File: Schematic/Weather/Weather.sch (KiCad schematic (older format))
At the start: 0 parts

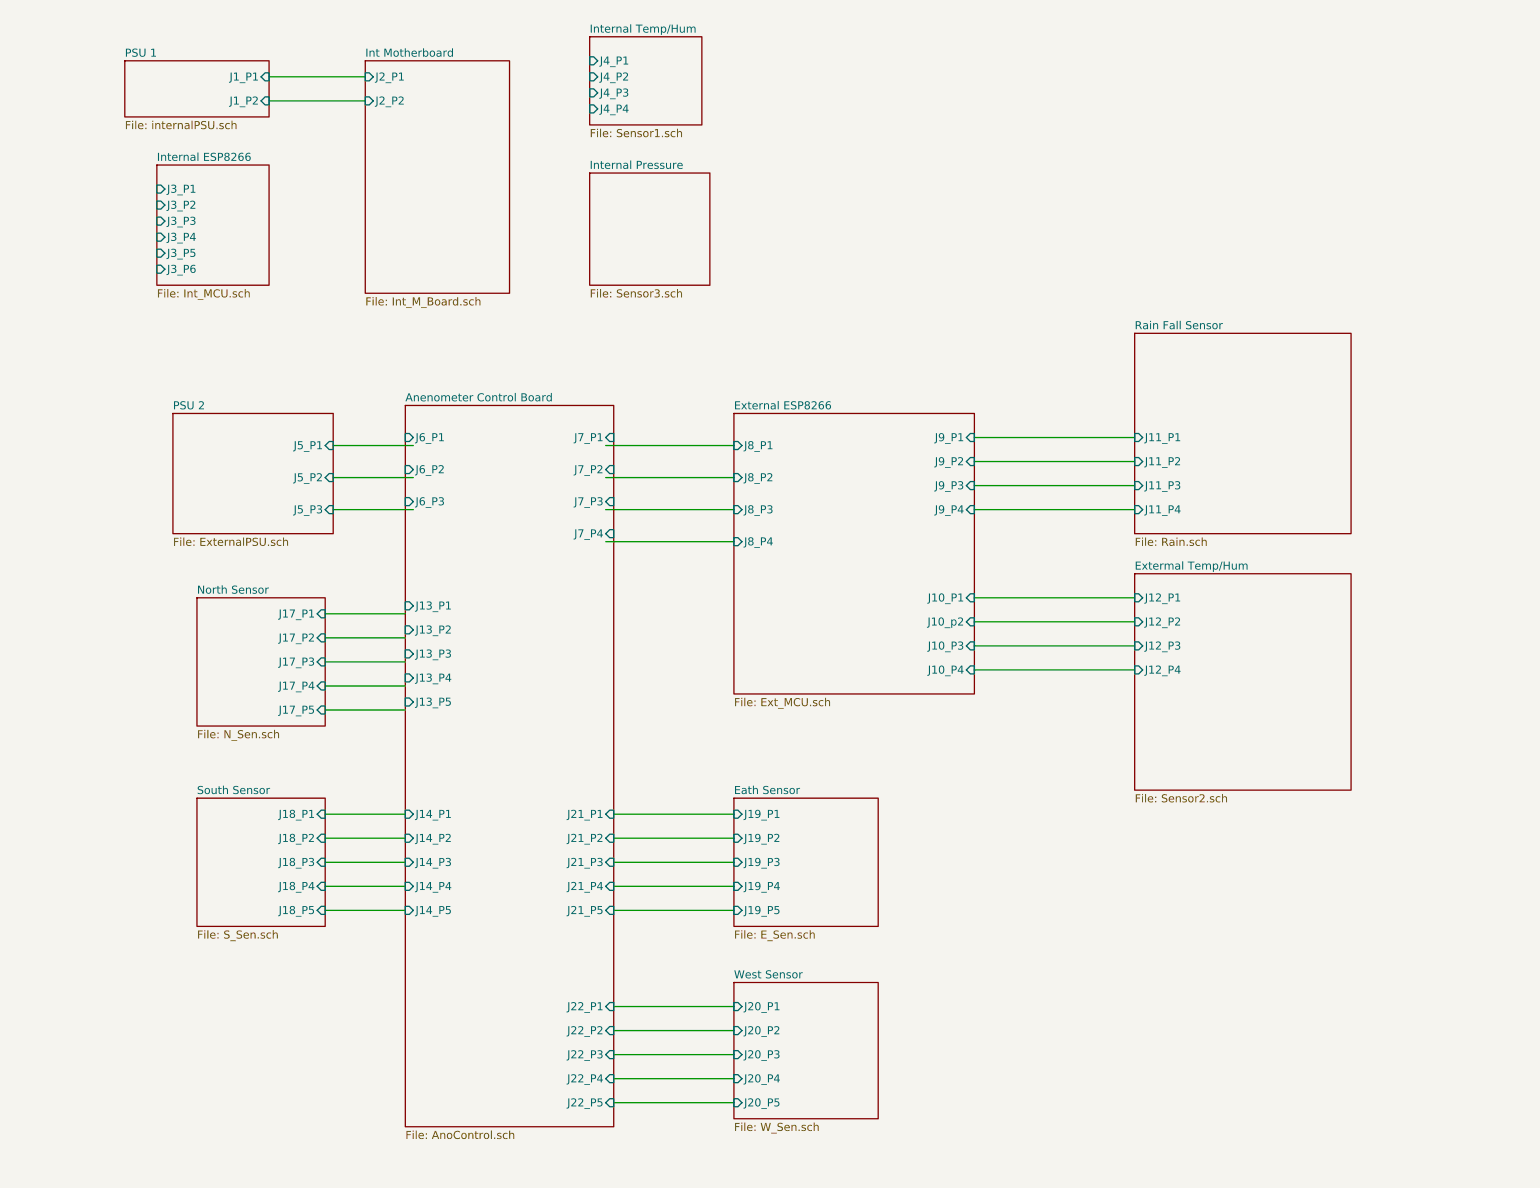
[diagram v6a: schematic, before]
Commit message: Connector relable start
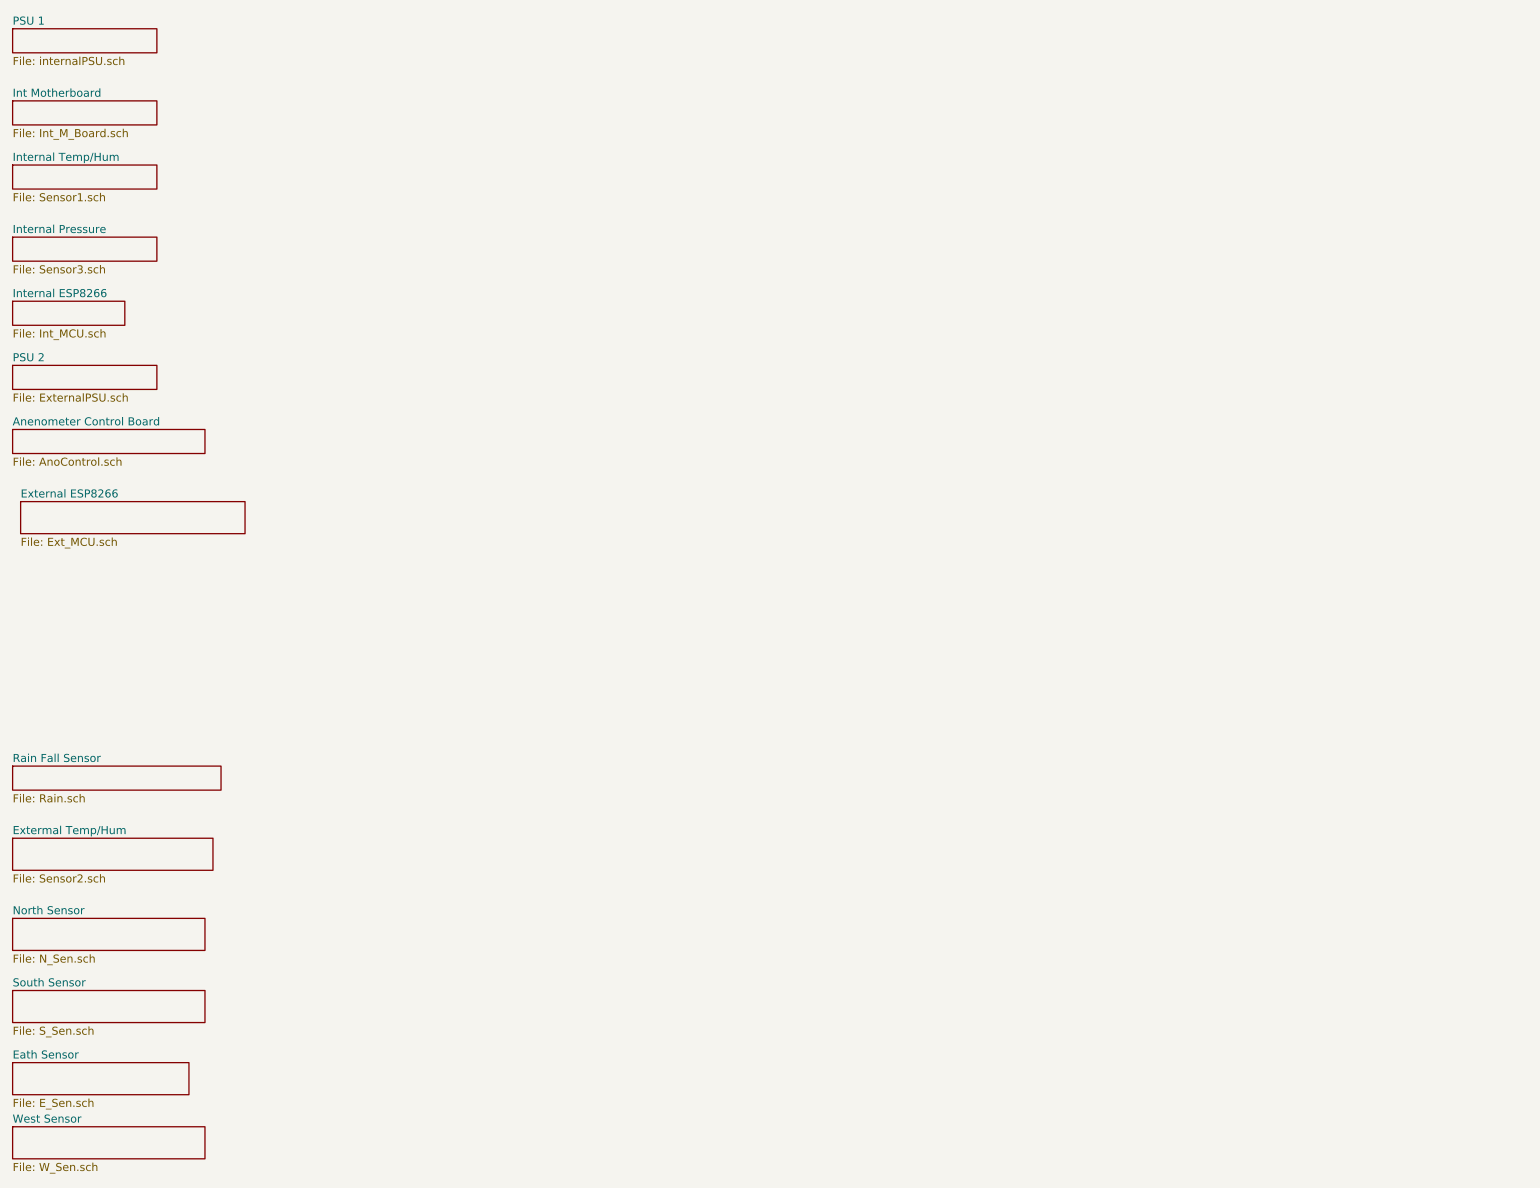
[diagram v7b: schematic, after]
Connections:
- wire segments 37 -> 0
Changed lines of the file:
@@
 $EndDescr
 $Sheet
-S 1200 800  900  350
+S 500  600  900  150
 U 5C9252D8
 F0 "PSU 1" 50
 F1 "internalPSU.sch" 50
-F2 "J1_P1" I R 2100 900 50
-F3 "J1_P2" I R 2100 1050 50
 $EndSheet
 $Sheet
-S 1400 1450 700  750
+S 500  2300 700  150
 U 5C9253D5
 F0 "Internal ESP8266" 50
 F1 "Int_MCU.sch" 50
-F2 "J3_P1" I L 1400 1600 50
-F3 "J3_P2" I L 1400 1700 50
-F4 "J3_P3" I L 1400 1800 50
-F5 "J3_P4" I L 1400 1900 50
-F6 "J3_P6" I L 1400 2100 50
-F7 "J3_P5" I L 1400 2000 50
 $EndSheet
 $Sheet
-S 4100 650  700  550
+S 500  1450 900  150
 U 5C9254A0
 F0 "Internal Temp/Hum" 50
 F1 "Sensor1.sch" 50
-F2 "J4_P1" I L 4100 800 50
-F3 "J4_P2" I L 4100 900 50
-F4 "J4_P3" I L 4100 1000 50
-F5 "J4_P4" I L 4100 1100 50
 $EndSheet
 $Sheet
-S 1500 3000 1000 750
+S 500  2700 900  150
 U 5C9638C4
 F0 "PSU 2" 50
 F1 "ExternalPSU.sch" 50
-F2 "J5_P1" I R 2500 3200 50
-F3 "J5_P2" I R 2500 3400 50
-F4 "J5_P3" I R 2500 3600 50
 $EndSheet
-Wire Wire Line
-	2500 3200 3000 3200
-Wire Wire Line
-	2500 3400 3000 3400
-Wire Wire Line
-	2500 3600 3000 3600
 $Sheet
-S 5000 3000 1500 1750
+S 550  3550 1400 200
 U 5C93D4CF
 F0 "External ESP8266" 50
 F1 "Ext_MCU.sch" 50
-F2 "J8_P1" I L 5000 3200 50
-F3 "J8_P2" I L 5000 3400 50
-F4 "J8_P3" I L 5000 3600 50
-F5 "J8_P4" I L 5000 3800 50
-F6 "J9_P1" I R 6500 3150 50
-F7 "J9_P2" I R 6500 3300 50
-F8 "J9_P3" I R 6500 3450 50
-F9 "J9_P4" I R 6500 3600 50
-F10 "J10_P1" I R 6500 4150 50
-F11 "J10_p2" I R 6500 4300 50
-F12 "J10_P3" I R 6500 4450 50
-F13 "J10_P4" I R 6500 4600 50
-$EndSheet
-Wire Wire Line
-	4200 3200 5000 3200
-Wire Wire Line
-	4200 3400 5000 3400
-Wire Wire Line
-	4200 3600 5000 3600
-Wire Wire Line
-	4200 3800 5000 3800
-$Sheet
-S 7500 2500 1350 1250
-U 5C93F504
-F0 "Rain Fall Sensor" 50
-F1 "Rain.sch" 50
-F2 "J11_P1" I L 7500 3150 50
-F3 "J11_P2" I L 7500 3300 50
-F4 "J11_P3" I L 7500 3450 50
-F5 "J11_P4" I L 7500 3600 50
 $EndSheet
 $Sheet
-S 7500 4000 1350 1350
-U 5C93F792
-F0 "Extermal Temp/Hum" 50
-F1 "Sensor2.sch" 50
-F2 "J12_P1" I L 7500 4150 50
-F3 "J12_P2" I L 7500 4300 50
-F4 "J12_P3" I L 7500 4450 50
-F5 "J12_P4" I L 7500 4600 50
-$EndSheet
-Wire Wire Line
-	6500 3150 7500 3150
-Wire Wire Line
-	6500 3300 7500 3300
-Wire Wire Line
-	6500 3450 7500 3450
-Wire Wire Line
-	6500 3600 7500 3600
-Wire Wire Line
-	6500 4150 7500 4150
-Wire Wire Line
-	6500 4300 7500 4300
-Wire Wire Line
-	6500 4450 7500 4450
-Wire Wire Line
-	6500 4600 7500 4600
-Wire Wire Line
-	2450 4250 2950 4250
-Wire Wire Line
-	2450 4550 2950 4550
-Wire Wire Line
-	2450 4400 2950 4400
-Wire Wire Line
-	2450 4700 2950 4700
-Wire Wire Line
-	2450 4850 2950 4850
-$Sheet
-S 1650 4150 800  800
+S 500  6150 1200 200
 U 5C952539
 F0 "North Sensor" 50
 F1 "N_Sen.sch" 50
-F2 "J17_P1" I R 2450 4250 50
-F3 "J17_P2" I R 2450 4400 50
-F4 "J17_P3" I R 2450 4550 50
-F5 "J17_P4" I R 2450 4700 50
-F6 "J17_P5" I R 2450 4850 50
 $EndSheet
 $Sheet
-S 1650 5400 800  800
+S 500  6600 1200 200
 U 5C9F4D88
 F0 "South Sensor" 50
 F1 "S_Sen.sch" 50
-F2 "J18_P1" I R 2450 5500 50
-F3 "J18_P2" I R 2450 5650 50
-F4 "J18_P3" I R 2450 5800 50
-F5 "J18_P4" I R 2450 5950 50
-F6 "J18_P5" I R 2450 6100 50
 $EndSheet
 $Sheet
-S 2950 2950 1300 4500
-U 5C96824E
-F0 "Anenometer Control Board" 50
-F1 "AnoControl.sch" 50
-F2 "J6_P1" I L 2950 3150 50
-F3 "J6_P2" I L 2950 3350 50
-F4 "J6_P3" I L 2950 3550 50
-F5 "J7_P1" I R 4250 3150 50
-F6 "J7_P2" I R 4250 3350 50
-F7 "J7_P3" I R 4250 3550 50
-F8 "J7_P4" I R 4250 3750 50
-F9 "J13_P1" I L 2950 4200 50
-F10 "J13_P2" I L 2950 4350 50
-F11 "J13_P3" I L 2950 4500 50
-F12 "J13_P4" I L 2950 4650 50
-F13 "J13_P5" I L 2950 4800 50
-F14 "J14_P1" I L 2950 5500 50
-F15 "J14_P2" I L 2950 5650 50
-F16 "J14_P3" I L 2950 5800 50
-F17 "J14_P4" I L 2950 5950 50
-F18 "J14_P5" I L 2950 6100 50
-F19 "J21_P1" I R 4250 5500 50
-F20 "J21_P2" I R 4250 5650 50
-F21 "J21_P3" I R 4250 5800 50
-F22 "J21_P4" I R 4250 5950 50
-F23 "J21_P5" I R 4250 6100 50
-F24 "J22_P1" I R 4250 6700 50
-F25 "J22_P2" I R 4250 6850 50
-F26 "J22_P3" I R 4250 7000 50
-F27 "J22_P4" I R 4250 7150 50
-F28 "J22_P5" I R 4250 7300 50
-$EndSheet
-Wire Wire Line
-	2450 5500 2950 5500
-Wire Wire Line
-	2450 5650 2950 5650
-Wire Wire Line
-	2450 5800 2950 5800
-Wire Wire Line
-	2450 5950 2950 5950
-Wire Wire Line
-	2450 6100 2950 6100
-$Sheet
-S 5000 5400 900  800
+S 500  7050 1100 200
 U 5CAC04D1
 F0 "Eath Sensor" 50
 F1 "E_Sen.sch" 50
-F2 "J19_P1" I L 5000 5500 50
-F3 "J19_P2" I L 5000 5650 50
-F4 "J19_P3" I L 5000 5800 50
-F5 "J19_P4" I L 5000 5950 50
-F6 "J19_P5" I L 5000 6100 50
 $EndSheet
 $Sheet
-S 5000 6550 900  850
+S 500  7450 1200 200
 U 5CAC05F6
 F0 "West Sensor" 50
 F1 "W_Sen.sch" 50
-F2 "J20_P1" I L 5000 6700 50
-F3 "J20_P2" I L 5000 6850 50
-F4 "J20_P3" I L 5000 7000 50
-F5 "J20_P4" I L 5000 7150 50
-F6 "J20_P5" I L 5000 7300 50
 $EndSheet
-Wire Wire Line
-	4250 5500 5000 5500
-Wire Wire Line
-	4250 5650 5000 5650
-Wire Wire Line
-	4250 5800 5000 5800
-Wire Wire Line
-	4250 5950 5000 5950
-Wire Wire Line
-	4250 6100 5000 6100
-Wire Wire Line
-	4250 6700 5000 6700
-Wire Wire Line
-	4250 6850 5000 6850
-Wire Wire Line
-	4250 7000 5000 7000
-Wire Wire Line
-	4250 7150 5000 7150
-Wire Wire Line
-	4250 7300 5000 7300
 $Sheet
-S 2700 800  900  1450
+S 500  1050 900  150
 U 5CAF7F5D
 F0 "Int Motherboard" 50
 F1 "Int_M_Board.sch" 50
-F2 "J2_P1" I L 2700 900 50
-F3 "J2_P2" I L 2700 1050 50
 $EndSheet
-Wire Wire Line
-	2100 900  2700 900
-Wire Wire Line
-	2100 1050 2700 1050
 $Sheet
-S 4100 1500 750  700
+S 500  1900 900  150
 U 5CB297E4
 F0 "Internal Pressure" 50
 F1 "Sensor3.sch" 50
 $EndSheet
+$Sheet
+S 500  3100 1200 150
+U 5C96824E
+F0 "Anenometer Control Board" 50
+F1 "AnoControl.sch" 50
+$EndSheet
+$Sheet
+S 500  5650 1250 200
+U 5C93F792
+F0 "Extermal Temp/Hum" 50
+F1 "Sensor2.sch" 50
+$EndSheet
+$Sheet
+S 500  5200 1300 150
+U 5C93F504
+F0 "Rain Fall Sensor" 50
+F1 "Rain.sch" 50
+$EndSheet
 $EndSCHEMATC

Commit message: Connector changes
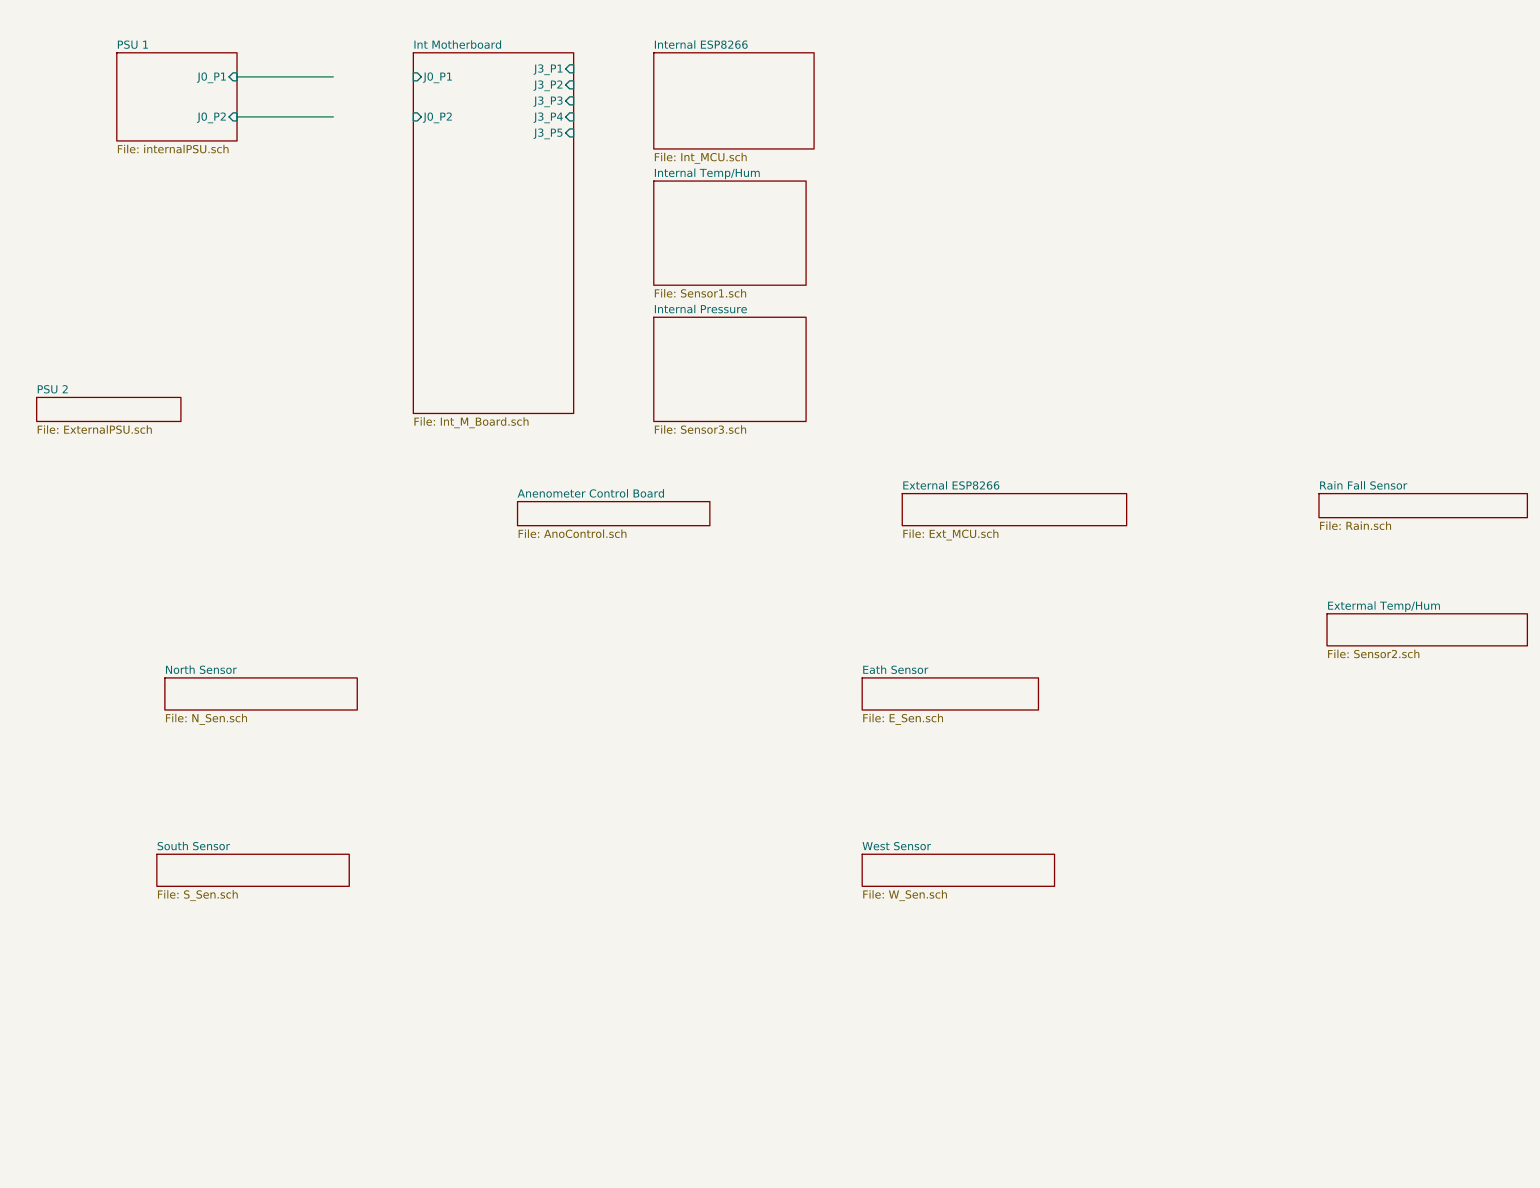
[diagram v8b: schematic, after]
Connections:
- wire segments 0 -> 2
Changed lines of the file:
@@
 $EndDescr
 $Sheet
-S 500  600  900  150
+S 1150 750  750  550
 U 5C9252D8
 F0 "PSU 1" 50
 F1 "internalPSU.sch" 50
+F2 "J0_P1" I R 1900 900 50
+F3 "J0_P2" I R 1900 1150 50
 $EndSheet
 $Sheet
-S 500  2300 700  150
+S 4500 750  1000 600
 U 5C9253D5
 F0 "Internal ESP8266" 50
@@
 $EndSheet
 $Sheet
-S 500  1450 900  150
+S 4500 1550 950  650
 U 5C9254A0
 F0 "Internal Temp/Hum" 50
@@
 $EndSheet
 $Sheet
-S 500  2700 900  150
+S 650  2900 900  150
 U 5C9638C4
 F0 "PSU 2" 50
@@
 $EndSheet
 $Sheet
-S 550  3550 1400 200
+S 6050 3500 1400 200
 U 5C93D4CF
 F0 "External ESP8266" 50
@@
 $EndSheet
 $Sheet
-S 500  6150 1200 200
+S 1450 4650 1200 200
 U 5C952539
 F0 "North Sensor" 50
@@
 $EndSheet
 $Sheet
-S 500  6600 1200 200
+S 1400 5750 1200 200
 U 5C9F4D88
 F0 "South Sensor" 50
@@
 $EndSheet
 $Sheet
-S 500  7050 1100 200
+S 5800 4650 1100 200
 U 5CAC04D1
 F0 "Eath Sensor" 50
@@
 $EndSheet
 $Sheet
-S 500  7450 1200 200
+S 5800 5750 1200 200
 U 5CAC05F6
 F0 "West Sensor" 50
@@
 $EndSheet
 $Sheet
-S 500  1050 900  150
+S 3000 750  1000 2250
 U 5CAF7F5D
 F0 "Int Motherboard" 50
 F1 "Int_M_Board.sch" 50
+F2 "J0_P1" I L 3000 900 50
+F3 "J0_P2" I L 3000 1150 50
+F4 "J3_P1" I R 4000 850 50
+F5 "J3_P2" I R 4000 950 50
+F6 "J3_P3" I R 4000 1050 50
+F7 "J3_P4" I R 4000 1150 50
+F8 "J3_P5" I R 4000 1250 50
 $EndSheet
 $Sheet
-S 500  1900 900  150
+S 4500 2400 950  650
 U 5CB297E4
 F0 "Internal Pressure" 50
@@
 $EndSheet
 $Sheet
-S 500  3100 1200 150
+S 3650 3550 1200 150
 U 5C96824E
 F0 "Anenometer Control Board" 50
@@
 $EndSheet
 $Sheet
-S 500  5650 1250 200
+S 8700 4250 1250 200
 U 5C93F792
 F0 "Extermal Temp/Hum" 50
@@
 $EndSheet
 $Sheet
-S 500  5200 1300 150
+S 8650 3500 1300 150
 U 5C93F504
 F0 "Rain Fall Sensor" 50
 F1 "Rain.sch" 50
 $EndSheet
+Wire Wire Line
+	1900 900  2500 900
+Wire Wire Line
+	1900 1150 2500 1150
 $EndSCHEMATC
